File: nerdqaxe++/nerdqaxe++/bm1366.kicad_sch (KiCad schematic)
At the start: 78 parts, among them J2 Conn_01x06, U19 BM1370_mode1, U20 BM1370_mode1, U25 BM1370_mode1, U26 BM1370_mode1, U35 TXU0304PW, U8 25MHz

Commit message: DFM
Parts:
- removed C11, C13, C15, C17: 100µ/6.3V, Capacitor_SMD:C_1210_3225Metric, symbol Device:C
- removed C26, C27, C29, C31: 10µ, Capacitor_SMD:C_0805_2012Metric, symbol Device:C
- removed C33, C38, C41, C46: 1µ, Capacitor_SMD:C_0805_2012Metric, symbol Device:C
- removed C49, C53, C55, C59: 100n, Capacitor_SMD:C_0805_2012Metric, symbol Device:C
- added C127, C128, C131, C132, C133, C134, C136, C137, C138, C139, C140, C81, C86, C89, C90, C91, C95, C97, C98, C99: 10uF, Capacitor_SMD:C_0603_1608Metric, symbol Device:C_Small
- C25, C82, C83: value 100n -> 100nF; footprint Capacitor_SMD:C_0805_2012Metric -> Capacitor_SMD:C_0402_1005Metric
- C28, C30, C32, C34, C35, C36, C37, C40, C42, C43, C44, C47, C50, C51, C52, C54, C56, C57, C58, C60, C62, C63, C64, C66, C67, C68, C69, C70, C71, C72, C73, C74, C75, C76, C77, C78, C79, C80, C93, C94: value 1µ -> 1µF; footprint Capacitor_SMD:C_0805_2012Metric -> Capacitor_SMD:C_0402_1005Metric
- R19, R20, R21, R22, R23, R44, R45, R46, R47, R49, R50, R51: footprint Resistor_SMD:R_0805_2012Metric -> Resistor_SMD:R_0402_1005Metric
- U35: Manufacturer TXU0304PWR -> (none); PARTNO (none) -> TXU0304PWR
- U8: Manufacturer LFSPXO076024REEL -> (none); PARTNO (none) -> LFSPXO076024REEL
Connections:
- net GND: now also C127.2, C128.2, C131.2, C132.2, C133.2, C134.2, C136.2, C137.2, C138.2, C139.2, C140.2, C81.2, C86.2, C89.2, C90.2, C91.2, C95.2, C97.2, C98.2, C99.2
- net VDD: now also C127.1, C128.1, C131.1, C132.1, C133.1, C134.1, C136.1, C137.1, C138.1, C139.1, C140.1, C81.1, C86.1, C89.1, C90.1, C91.1, C95.1, C97.1, C98.1, C99.1

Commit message: 5v
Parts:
- C127, C128, C131, C132, C133, C134, C136, C137, C138, C139, C140, C81, C86, C89, C90, C91, C95, C97, C98, C99: DK 490-18214-1-ND -> (none); Voltage 25V -> (none)
- C25, C82, C83: PARTNO (none) -> CL05A104KO5NNNC
- C28, C30, C32, C34, C35, C36, C37, C40, C42, C43, C44, C47, C50, C51, C52, C54, C56, C57, C58, C60, C62, C63, C64, C66, C67, C68, C69, C70, C71, C72, C73, C74, C75, C76, C77, C78, C79, C80, C93, C94: PARTNO (none) -> EMK105BJ105MV-F
- R19, R20, R21, R22, R23: PARTNO (none) -> RC0402JR-0710KL
- R44, R45, R46, R47: PARTNO (none) -> RC0402FR-071KL
- U8: PARTNO LFSPXO076024REEL -> SX3M25.000E20F30THN

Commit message: finishing up
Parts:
- C127, C128, C131, C132, C133, C134, C136, C137, C138, C139, C140, C81, C86, C89, C90, C91, C95, C97, C98, C99: LCSC (none) -> C92487 Hot; Manufacturer  (none) -> Samsung Electro-Mechanics; PARTNO GRM188R61E106KA73D -> CL10A106MO8NQNC
- C25, C82, C83: LCSC (none) -> C60474; Manufacturer  (none) -> YAGEO; PARTNO CL05A104KO5NNNC -> CC0402KRX7R7BB104
- C28, C30, C32, C34, C35, C36, C37, C40, C42, C43, C44, C47, C50, C51, C52, C54, C56, C57, C58, C60, C62, C63, C64, C66, C67, C68, C69, C70, C71, C72, C73, C74, C75, C76, C77, C78, C79, C80, C93, C94: LCSC (none) -> C29266; PARTNO EMK105BJ105MV-F -> CL05A105KO5NNNC
- R19, R20, R21, R22, R23: LCSC (none) -> C471764; Manufacturer  (none) -> YAGEO; PARTNO RC0402JR-0710KL -> RC0402DR-0710KL
- R44, R45, R46, R47: LCSC (none) -> C106235; Manufacturer  (none) -> YAGEO
- R49, R50, R51: LCSC (none) -> C60488; Manufacturer  (none) -> YAGEO; PARTNO (none) -> RC0402FR-072KL
- U19, U25, U26: footprint myfootprints:BM1370 -> qaxe:BM1370
- U20: value BM1370_mode1 -> BM1370; footprint myfootprints:BM1370 -> qaxe:BM1370
- U35: Manufacturer  (none) -> Texas Instruments
- U8: Manufacturer  (none) -> Shenzhen SCTF Elec

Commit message: level shifter
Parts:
- removed C82, C83: 100nF, Capacitor_SMD:C_0402_1005Metric, symbol Device:C
- removed U35: TXU0304PW, Package_SO:TSSOP-14_4.4x5mm_P0.65mm, symbol mylib7:TXU0304
- added C100, C59: 0.1uF, Capacitor_SMD:C_0402_1005Metric, symbol Device:C_Small
- added R26: 20k, Resistor_SMD:R_0402_1005Metric, symbol Device:R_Small_US
- added U6: SN74AVC4T774, qaxe:BQB0016A-MFG, symbol bitaxe:SN74AVC4T774-BQB
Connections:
- net +1V2: now also C59.1, U6.16 (VCCA), U6.7 (DIR3), U6.8 (DIR4)
- net +3V3: now also C100.1, U6.15 (VCCB)
- net CI: now also U6.5 (A3)
- net GND: now also C100.2, C59.2, R26.1, U6.1 (DIR1), U6.10 (GND), U6.2 (DIR2), U6.6 (A4)
- net RESET: now also U6.13 (B2)
- net RO: now also U6.3 (A1)
- net RST_N: now also U6.4 (A2)
- net RXD: now also U6.14 (B1)
- net TXD: now also U6.12 (B3)
- new net: R26.2, U6.9 (OE)

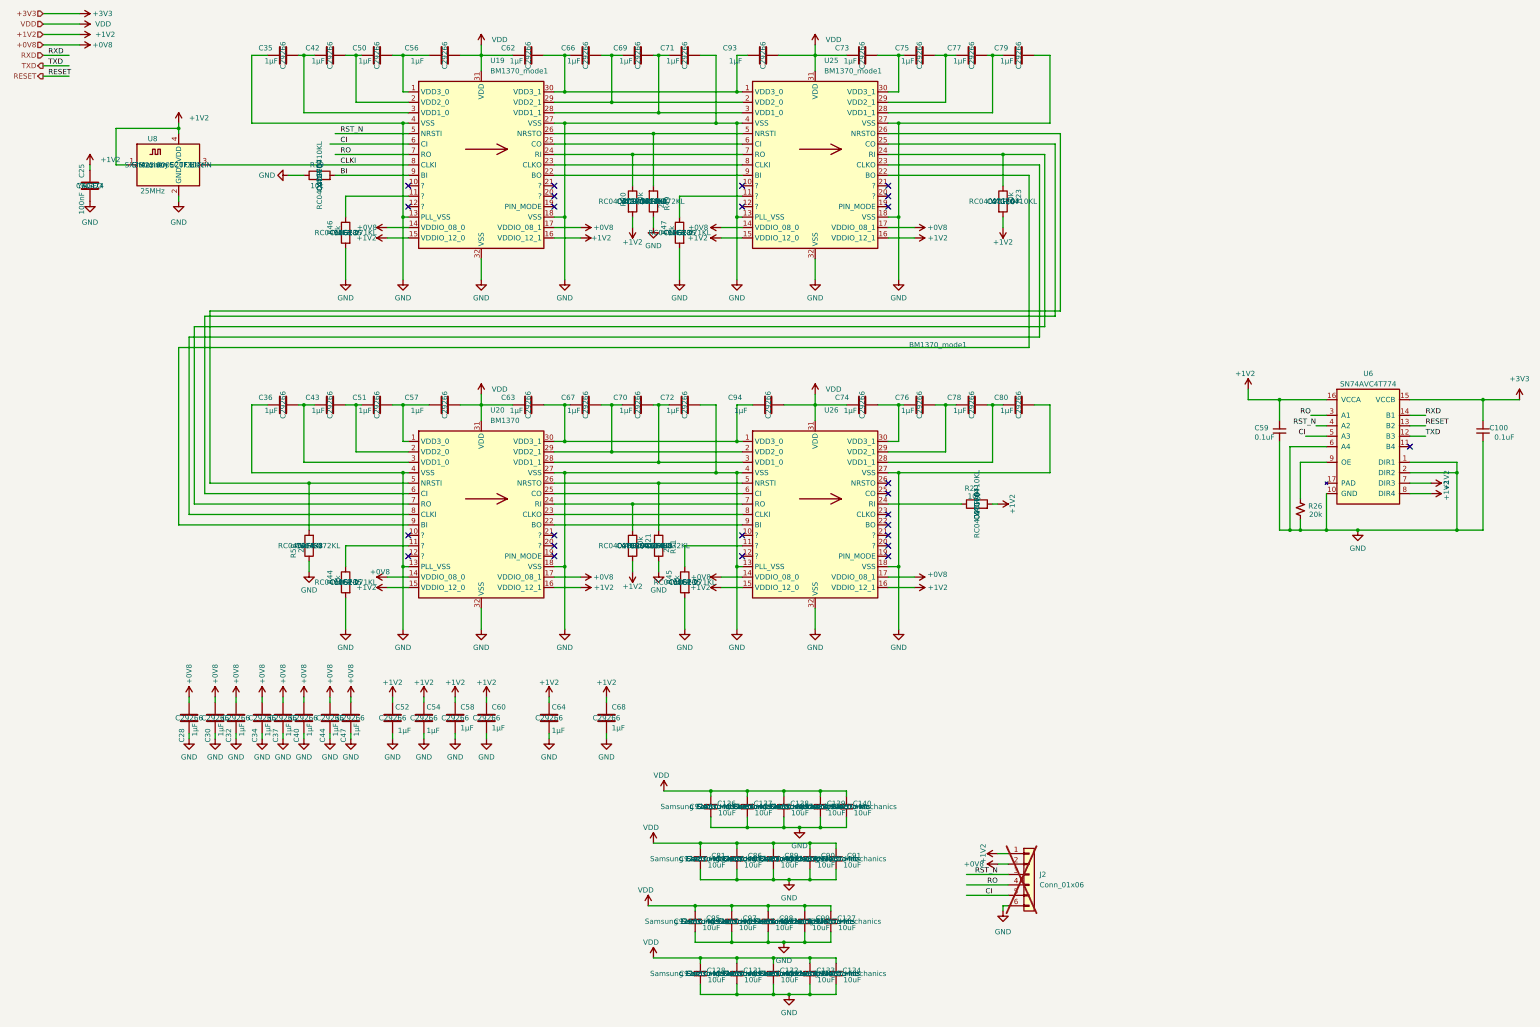
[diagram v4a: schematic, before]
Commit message: hide unnecessary fields in schematic
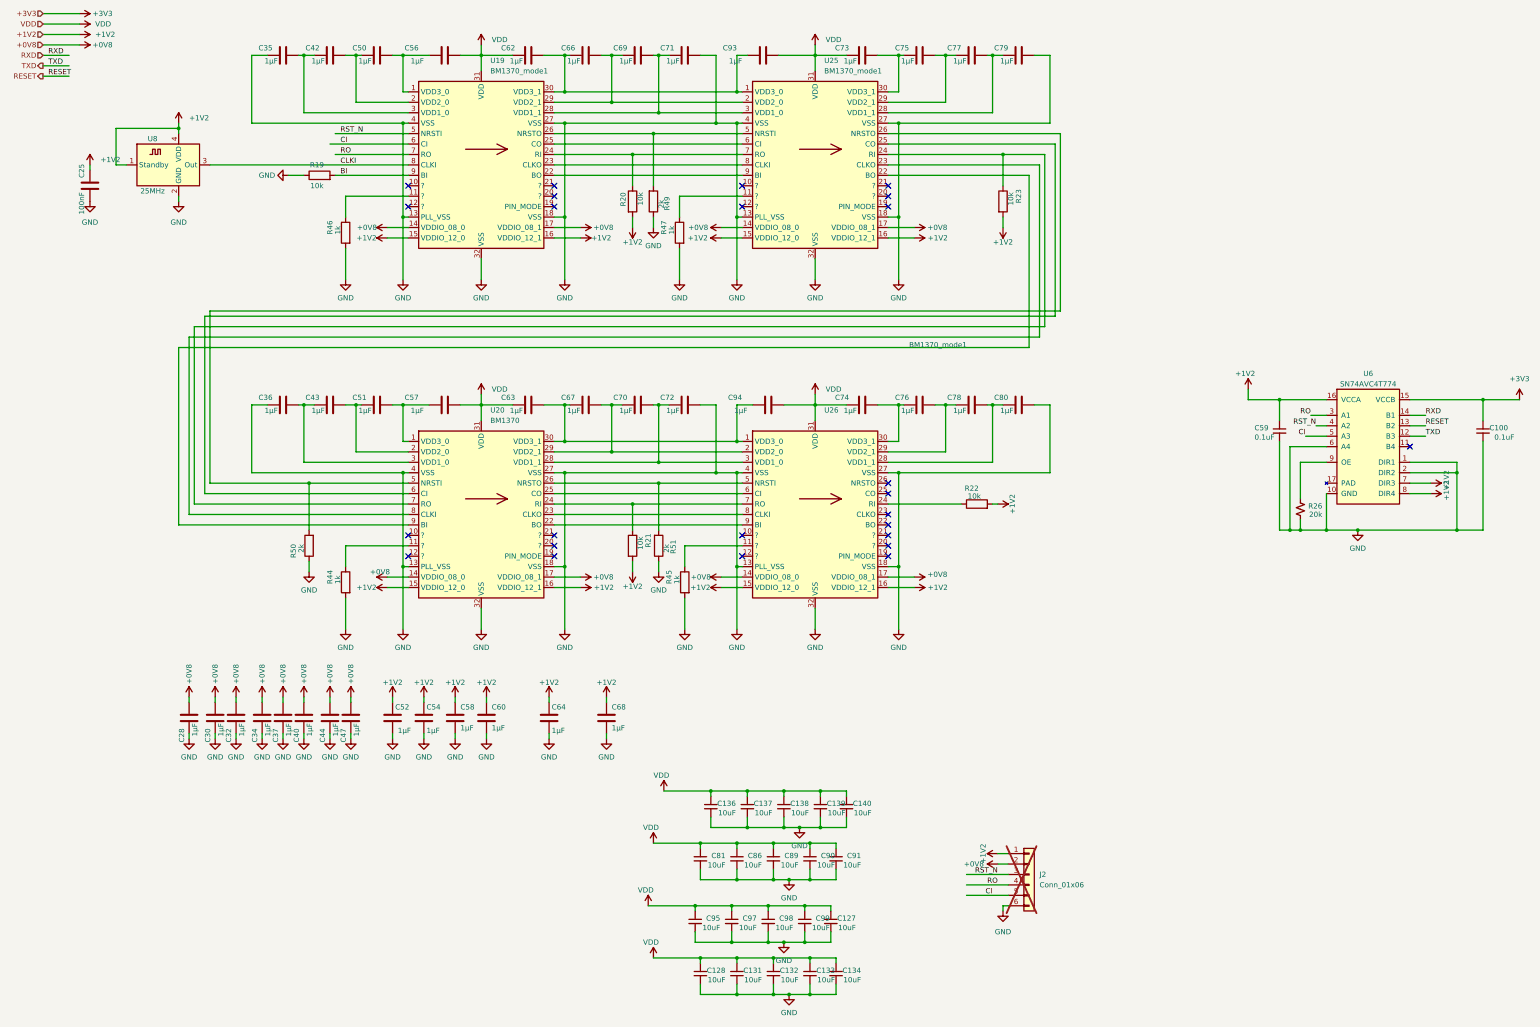
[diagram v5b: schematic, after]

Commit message: schematic values cleanup
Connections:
- no-connect marks 25 -> 26
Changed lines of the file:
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@@
 	)
 	(junction
+		(at 376.555 157.48)
+		(diameter 0)
+		(color 0 0 0 0)
+	)
+	(junction
 		(at 209.55 257.81)
 		(diameter 0)
@@
 	)
 	(junction
-		(at 373.38 157.48)
-		(diameter 0)
-		(color 0 0 0 0)
-	)
-	(junction
 		(at 198.12 135.89)
 		(diameter 0)
@@
 	)
 	(junction
+		(at 376.555 143.51)
+		(diameter 0)
+		(color 0 0 0 0)
+	)
+	(junction
 		(at 177.8 60.96)
 		(diameter 0)
@@
 	)
 	(junction
-		(at 373.38 143.51)
-		(diameter 0)
-		(color 0 0 0 0)
-	)
-	(junction
 		(at 260.35 127)
 		(diameter 0)
@@
 		(at 234.95 76.2)
 	)
+	(no_connect
+		(at 341.63 146.05)
+	)
 	(wire
 		(pts
@@
 	(wire
 		(pts
-			(xy 361.95 140.97) (xy 373.38 140.97)
+			(xy 361.95 140.97) (xy 376.555 140.97)
 		)
 		(stroke
@@
 	(wire
 		(pts
-			(xy 373.38 140.97) (xy 373.38 143.51)
+			(xy 376.555 140.97) (xy 376.555 143.51)
 		)
 		(stroke
@@
 	(wire
 		(pts
-			(xy 373.38 143.51) (xy 373.38 157.48)
+			(xy 376.555 143.51) (xy 376.555 157.48)
 		)
 		(stroke
@@
 	(wire
 		(pts
-			(xy 361.95 143.51) (xy 373.38 143.51)
+			(xy 361.95 143.51) (xy 376.555 143.51)
 		)
 		(stroke
@@
 	(wire
 		(pts
-			(xy 336.55 134.62) (xy 341.63 134.62)
+			(xy 337.82 134.62) (xy 341.63 134.62)
 		)
 		(stroke
@@
 	(wire
 		(pts
-			(xy 373.38 157.48) (xy 379.73 157.48)
-		)
-		(stroke
-			(width 0)
-			(type default)
-		)
-	)
-	(wire
-		(pts
 			(xy 193.04 143.51) (xy 193.04 127)
 		)
@@
 	(wire
 		(pts
-			(xy 349.25 157.48) (xy 373.38 157.48)
+			(xy 349.25 157.48) (xy 376.555 157.48)
 		)
 		(stroke
@@
 	(wire
 		(pts
+			(xy 376.555 157.48) (xy 379.73 157.48)
+		)
+		(stroke
+			(width 0)
+			(type default)
+		)
+	)
+	(wire
+		(pts
 			(xy 198.12 58.42) (xy 198.12 81.28)
 		)
@@
 	(wire
 		(pts
-			(xy 339.09 132.08) (xy 341.63 132.08)
+			(xy 337.82 132.08) (xy 341.63 132.08)
 		)
 		(stroke
@@
 	)
 	(label "CI"
-		(at 336.55 134.62 180)
+		(at 337.82 134.62 180)
 		(effects
 			(font
@@
 	)
 	(label "RST_N"
-		(at 339.09 132.08 180)
+		(at 337.82 132.08 180)
 		(effects
 			(font
@@
 		)
 		(property "Value" "+1V2"
-			(at 370.84 145.415 0)
+			(at 369.57 148.59 90)
 			(effects
 				(font
@@
 		)
 		(property "Value" "+1V2"
-			(at 370.84 142.875 0)
+			(at 369.57 146.05 90)
 			(effects
 				(font

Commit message: layout
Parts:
- removed J2: Conn_01x06, Connector_PinHeader_1.27mm:PinHeader_1x06_P1.27mm_Vertical, symbol Connector_Generic:Conn_01x06
- C28, C30, C32, C34, C35, C36, C37, C40, C42, C43, C44, C47, C50, C51, C52, C54, C56, C57, C58, C60, C62, C63, C64, C66, C67, C68, C69, C70, C71, C72, C73, C74, C75, C76, C77, C78, C79, C80, C93, C94: Manufacturer  (none) -> Samsung Electro-Mechanics
- R26: Manufacturer  (none) -> YAGEO
- U6: Manufacturer  (none) -> Texas Instruments

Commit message: Rev. 6.1
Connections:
- net +1V2: now also U6.1 (DIR1); no longer U6.7 (DIR3)
- net GND: now also U6.7 (DIR3); no longer U6.1 (DIR1)
- net RESET: now also U6.12 (B3); no longer U6.13 (B2)
- net TXD: now also U6.13 (B2); no longer U6.12 (B3)
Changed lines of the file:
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@@
 	)
 	(junction
-		(at 376.555 157.48)
-		(diameter 0)
-		(color 0 0 0 0)
-	)
-	(junction
 		(at 209.55 257.81)
 		(diameter 0)
@@
 	)
 	(junction
-		(at 198.12 233.68)
+		(at 379.73 143.51)
 		(diameter 0)
 		(color 0 0 0 0)
 	)
 	(junction
-		(at 200.66 229.87)
+		(at 198.12 233.68)
 		(diameter 0)
 		(color 0 0 0 0)
 	)
 	(junction
-		(at 196.85 257.81)
+		(at 200.66 229.87)
 		(diameter 0)
 		(color 0 0 0 0)
 	)
 	(junction
-		(at 376.555 143.51)
+		(at 196.85 257.81)
 		(diameter 0)
 		(color 0 0 0 0)
@@
 	)
 	(junction
+		(at 379.73 146.05)
+		(diameter 0)
+		(color 0 0 0 0)
+	)
+	(junction
 		(at 156.21 81.28)
 		(diameter 0)
@@
 	(wire
 		(pts
-			(xy 361.95 140.97) (xy 376.555 140.97)
-		)
-		(stroke
-			(width 0)
-			(type default)
-		)
-	)
-	(wire
-		(pts
 			(xy 151.13 127) (xy 156.21 127)
 		)
@@
 	(wire
 		(pts
-			(xy 376.555 140.97) (xy 376.555 143.51)
-		)
-		(stroke
-			(width 0)
-			(type default)
-		)
-	)
-	(wire
-		(pts
 			(xy 220.98 250.19) (xy 220.98 248.92)
 		)
@@
 	(wire
 		(pts
-			(xy 376.555 143.51) (xy 376.555 157.48)
-		)
-		(stroke
-			(width 0)
-			(type default)
-		)
-	)
-	(wire
-		(pts
 			(xy 179.07 55.88) (xy 179.07 41.91)
 		)
@@
 	(wire
 		(pts
+			(xy 349.25 157.48) (xy 379.73 157.48)
+		)
+		(stroke
+			(width 0)
+			(type default)
+		)
+	)
+	(wire
+		(pts
 			(xy 262.89 81.28) (xy 262.89 83.82)
 		)
@@
 	(wire
 		(pts
-			(xy 361.95 146.05) (xy 367.03 146.05)
-		)
-		(stroke
-			(width 0)
-			(type default)
-		)
-	)
-	(wire
-		(pts
 			(xy 118.11 161.29) (xy 102.87 161.29)
 		)
@@
 	(wire
 		(pts
-			(xy 361.95 143.51) (xy 376.555 143.51)
-		)
-		(stroke
-			(width 0)
-			(type default)
-		)
-	)
-	(wire
-		(pts
 			(xy 29.21 31.75) (xy 38.1 31.75)
 		)
@@
 	(wire
 		(pts
+			(xy 361.95 143.51) (xy 379.73 143.51)
+		)
+		(stroke
+			(width 0)
+			(type default)
+		)
+	)
+	(wire
+		(pts
 			(xy 156.21 135.89) (xy 198.12 135.89)
 		)
@@
 	(wire
 		(pts
+			(xy 361.95 140.97) (xy 367.03 140.97)
+		)
+		(stroke
+			(width 0)
+			(type default)
+		)
+	)
+	(wire
+		(pts
 			(xy 187.96 255.27) (xy 187.96 257.81)
 		)
@@
 	(wire
 		(pts
+			(xy 379.73 146.05) (xy 379.73 157.48)
+		)
+		(stroke
+			(width 0)
+			(type default)
+		)
+	)
+	(wire
+		(pts
 			(xy 191.77 227.33) (xy 191.77 229.87)
 		)
@@
 	(wire
 		(pts
-			(xy 379.73 135.89) (xy 379.73 157.48)
+			(xy 379.73 135.89) (xy 379.73 143.51)
 		)
 		(stroke
@@
 	(wire
 		(pts
+			(xy 379.73 143.51) (xy 379.73 146.05)
+		)
+		(stroke
+			(width 0)
+			(type default)
+		)
+	)
+	(wire
+		(pts
 			(xy 167.64 53.34) (xy 199.39 53.34)
 		)
@@
 	(wire
 		(pts
-			(xy 349.25 157.48) (xy 376.555 157.48)
+			(xy 135.89 39.37) (xy 135.89 41.91)
 		)
 		(stroke
@@
 	(wire
 		(pts
-			(xy 135.89 39.37) (xy 135.89 41.91)
+			(xy 260.35 41.91) (xy 262.89 41.91)
 		)
 		(stroke
@@
 	(wire
 		(pts
-			(xy 260.35 41.91) (xy 262.89 41.91)
+			(xy 207.01 242.57) (xy 210.82 242.57)
 		)
 		(stroke
@@
 	(wire
 		(pts
-			(xy 207.01 242.57) (xy 210.82 242.57)
+			(xy 104.14 198.12) (xy 104.14 199.39)
 		)
 		(stroke
@@
 	(wire
 		(pts
-			(xy 104.14 198.12) (xy 104.14 199.39)
+			(xy 102.87 76.2) (xy 118.11 76.2)
 		)
 		(stroke
@@
 	(wire
 		(pts
-			(xy 102.87 76.2) (xy 118.11 76.2)
+			(xy 361.95 146.05) (xy 379.73 146.05)
 		)
 		(stroke
@@
 	(wire
 		(pts
-			(xy 376.555 157.48) (xy 379.73 157.48)
-		)
-		(stroke
-			(width 0)
-			(type default)
-		)
-	)
-	(wire
-		(pts
 			(xy 198.12 58.42) (xy 198.12 81.28)
 		)
@@
 		)
 	)
-	(label "RESET"
-		(at 365.76 132.08 0)
-		(effects
-			(font
-				(size 1.27 1.27)
-			)
-			(justify left bottom)
-		)
-	)
 	(label "CI"
 		(at 337.82 134.62 180)
@@
 		)
 	)
-	(label "TXD"
-		(at 365.76 134.62 0)
-		(effects
-			(font
-				(size 1.27 1.27)
-			)
-			(justify left bottom)
-		)
-	)
 	(label "RXD"
 		(at 365.76 129.54 0)
@@
 		)
 	)
+	(label "TXD"
+		(at 365.76 132.08 0)
+		(effects
+			(font
+				(size 1.27 1.27)
+			)
+			(justify left bottom)
+		)
+	)
 	(label "RST_N"
 		(at 101.6 60.96 0)
@@
 		)
 	)
+	(label "RESET"
+		(at 365.76 134.62 0)
+		(effects
+			(font
+				(size 1.27 1.27)
+			)
+			(justify left bottom)
+		)
+	)
 	(label "RO"
 		(at 337.82 129.54 180)
@@
 	(symbol
 		(lib_id "power:+1V2")
-		(at 367.03 146.05 270)
+		(at 367.03 140.97 270)
 		(unit 1)
 		(exclude_from_sim no)
@@
 		(dnp no)
 		(property "Reference" "#PWR0177"
-			(at 363.22 146.05 0)
+			(at 363.22 140.97 0)
 			(effects
 				(font
@@
 		)
 		(property "Value" "+1V2"
-			(at 369.57 146.05 90)
+			(at 369.57 140.97 90)
 			(effects
 				(font
@@
 		)
 		(property "Footprint" ""
-			(at 367.03 146.05 0)
+			(at 367.03 140.97 0)
 			(effects
 				(font
@@
 		)
 		(property "Datasheet" ""
-			(at 367.03 146.05 0)
+			(at 367.03 140.97 0)
 			(effects
 				(font
@@
 		)
 		(property "Description" "Power symbol creates a global label with name \"+1V2\""
-			(at 367.03 146.05 0)
+			(at 367.03 140.97 0)
 			(effects
 				(font
